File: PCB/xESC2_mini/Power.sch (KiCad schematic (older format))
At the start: 20 parts, among them J10 Conn_01x06_Male, J9 Conn_01x06_Male, U1 TMC6200-TA

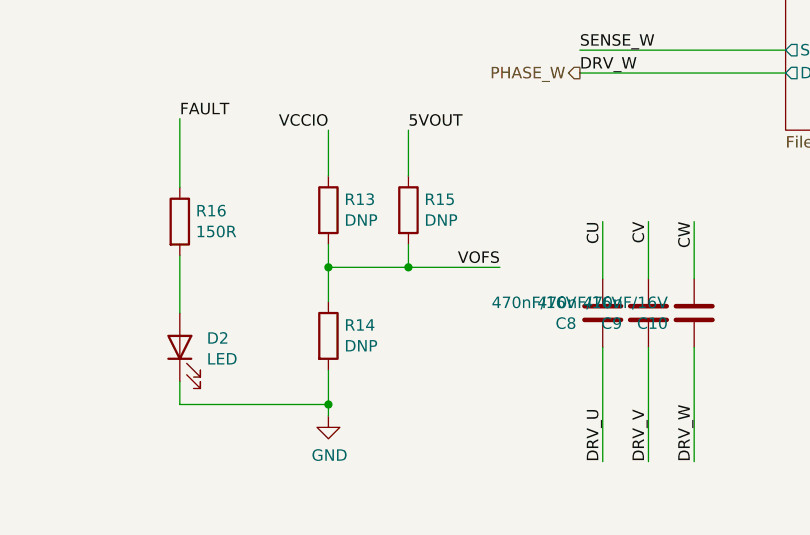
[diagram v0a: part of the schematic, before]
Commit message: added current bias resistors
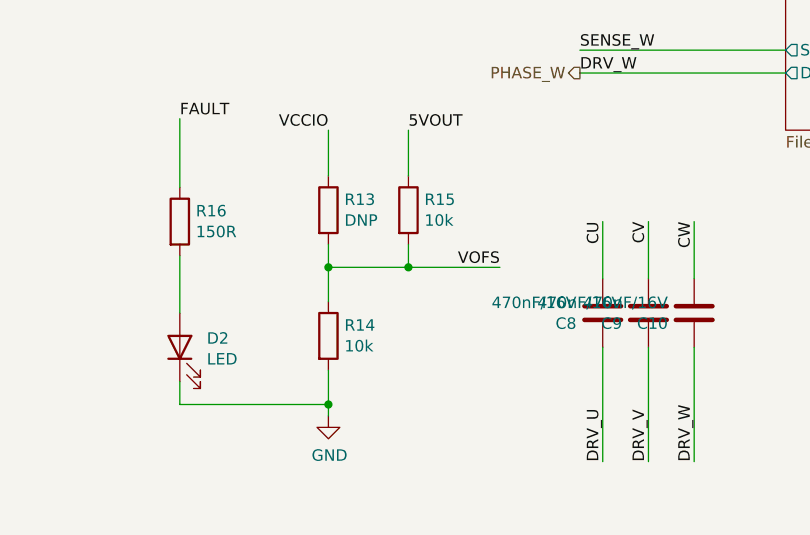
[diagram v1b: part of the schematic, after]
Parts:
- R14, R15: value DNP -> 10k
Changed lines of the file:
@@
 P 7950 5850
 F 0 "R14" H 8020 5896 50  0000 L CNN
-F 1 "DNP" H 8020 5805 50  0000 L CNN
+F 1 "10k" H 8020 5805 50  0000 L CNN
 F 2 "Resistor_SMD:R_0603_1608Metric" V 7880 5850 50  0001 C CNN
 F 3 "~" H 7950 5850 50  0001 C CNN
@@
 P 8300 5300
 F 0 "R15" H 8370 5346 50  0000 L CNN
-F 1 "DNP" H 8370 5255 50  0000 L CNN
+F 1 "10k" H 8370 5255 50  0000 L CNN
 F 2 "Resistor_SMD:R_0603_1608Metric" V 8230 5300 50  0001 C CNN
 F 3 "~" H 8300 5300 50  0001 C CNN
